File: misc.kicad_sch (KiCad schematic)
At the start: 23 parts, among them J7 Conn_ARM_JTAG_SWD_10, SW2 SW_DIP_x02, U1 MIMX8MM6DVTLZAA, Y3 24Mhz

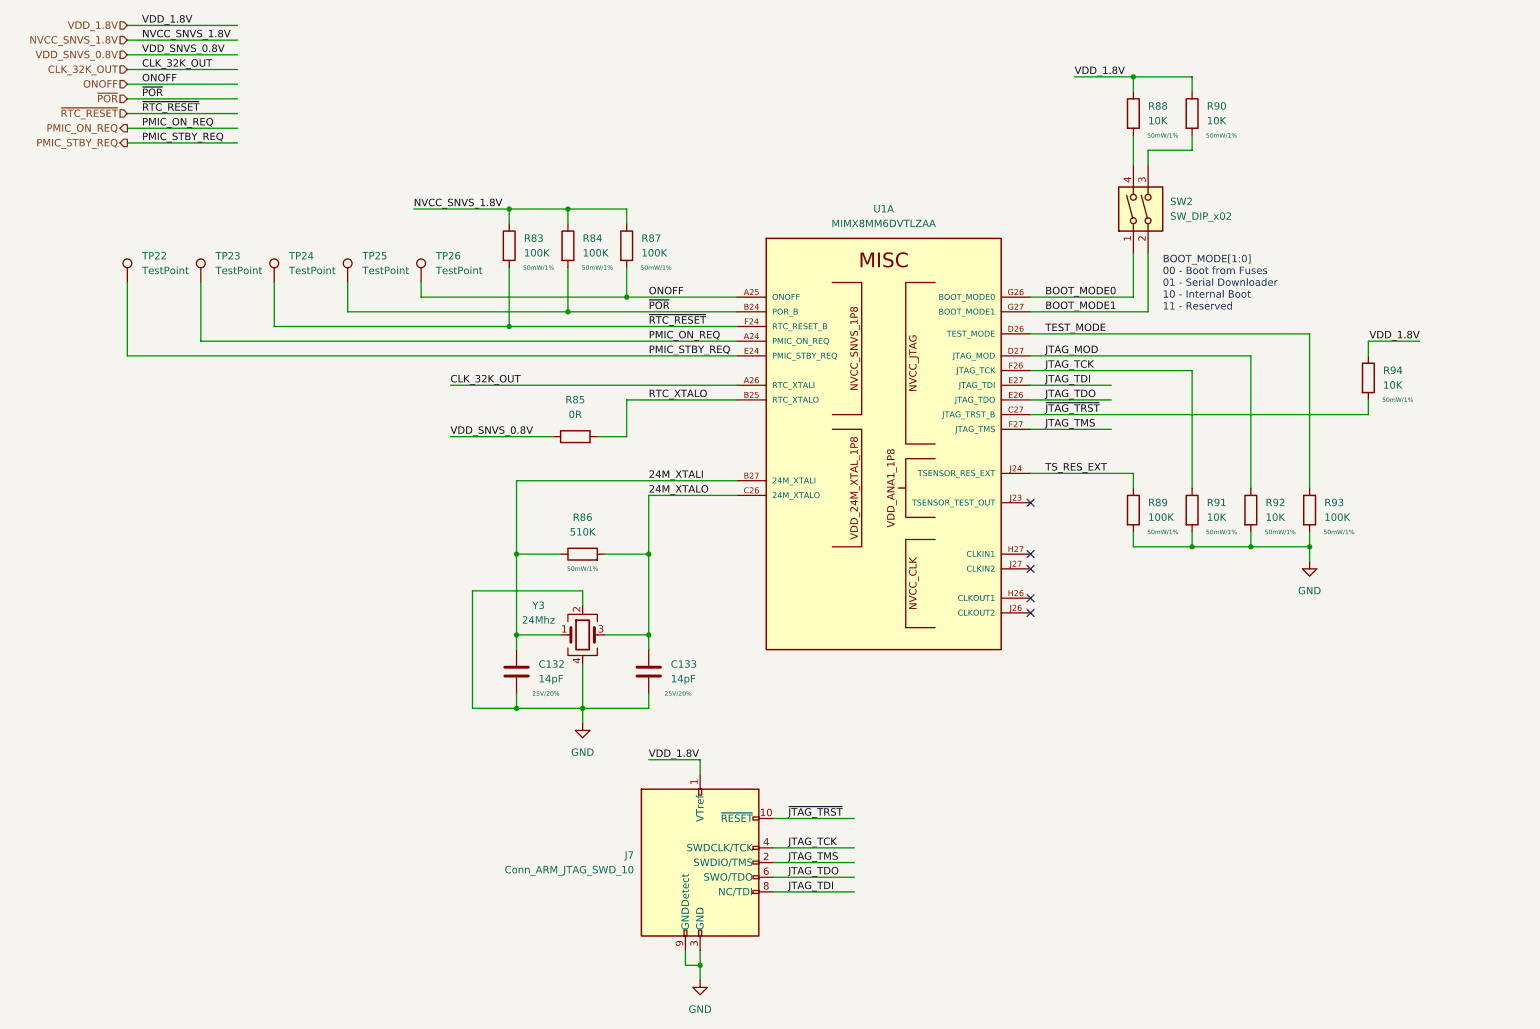
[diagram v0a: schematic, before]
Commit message: add SN65DSI86 DSI2DP ic, SCH, PCB work, flytime work
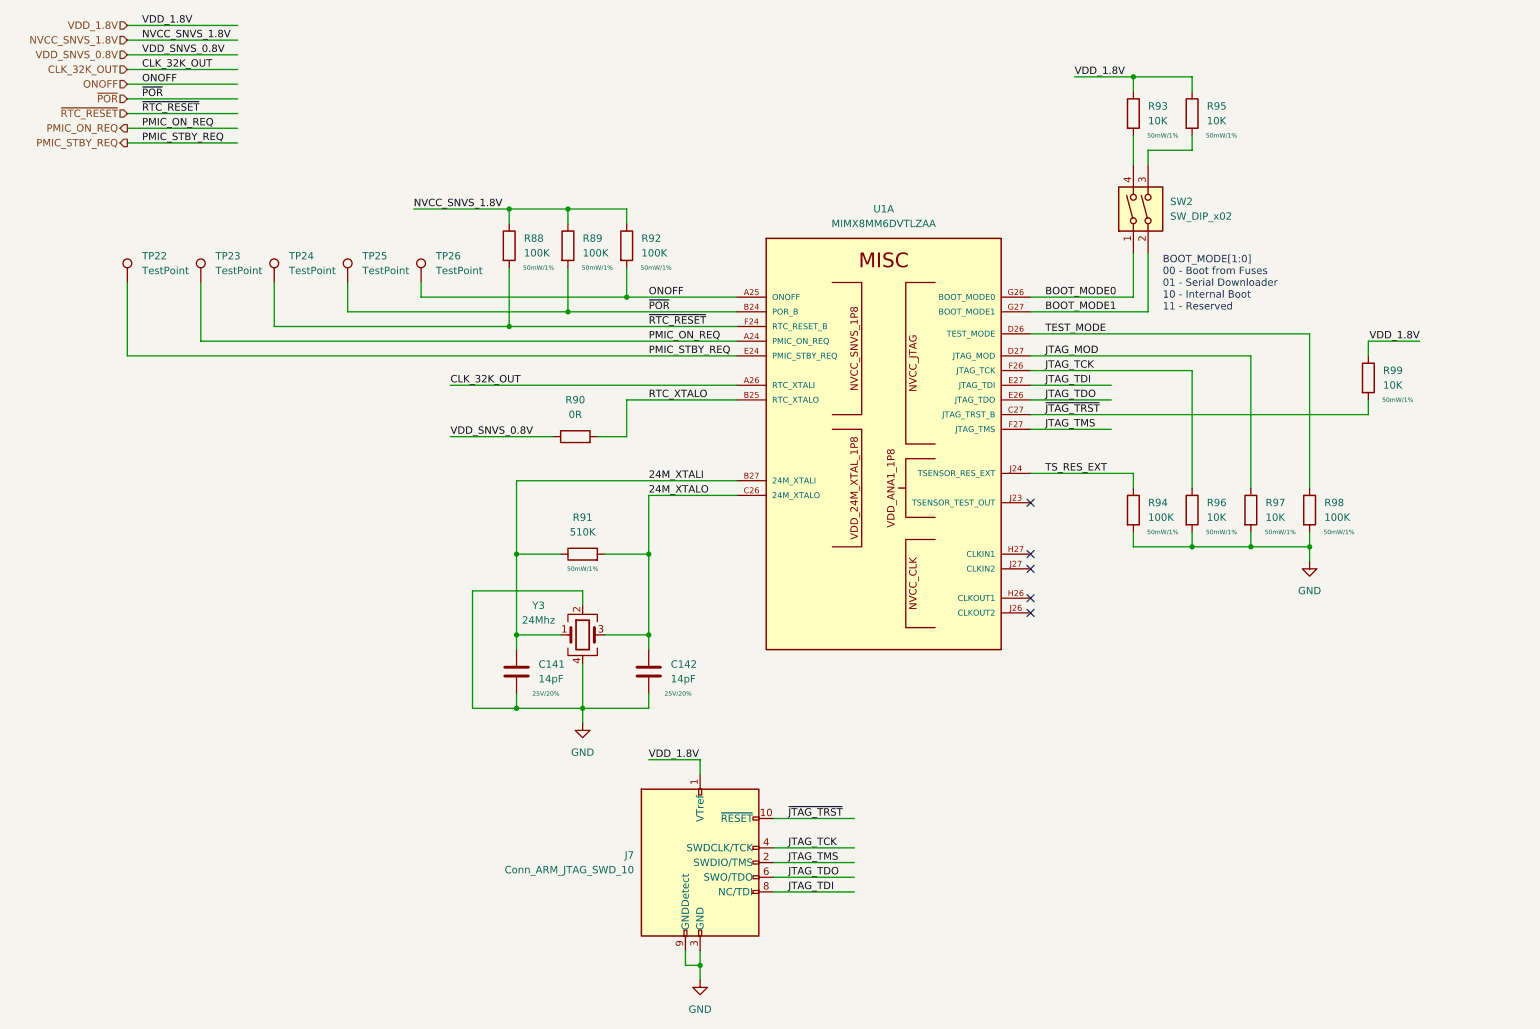
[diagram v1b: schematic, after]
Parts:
- renumbered C132 to C141, C133 to C142, R83 to R88, R84 to R89, R85 to R90, R86 to R91, R87 to R92, R88 to R93, R89 to R94, R90 to R95, R91 to R96, R92 to R97, R93 to R98, R94 to R99
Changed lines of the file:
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@@
   (symbol (lib_id "Device:C") (at 97.79 132.08 0) (unit 1)
     (in_bom yes) (on_board yes)
-    (property "Reference" "C132" (id 0) (at 101.6 130.8099 0)
+    (property "Reference" "C141" (id 0) (at 101.6 130.8099 0)
       (effects (font (size 1.27 1.27)) (justify left))
     )
@@
   (symbol (lib_id "Device:R") (at 224.79 104.14 0) (unit 1)
     (in_bom yes) (on_board yes)
-    (property "Reference" "R92" (id 0) (at 227.33 102.8699 0)
+    (property "Reference" "R97" (id 0) (at 227.33 102.8699 0)
       (effects (font (size 1.27 1.27)) (justify left))
     )
@@
   (symbol (lib_id "power:GND") (at 129.54 185.42 0) (unit 1)
     (in_bom yes) (on_board yes) (fields_autoplaced)
-    (property "Reference" "#PWR0128" (id 0) (at 129.54 191.77 0)
+    (property "Reference" "#PWR0132" (id 0) (at 129.54 191.77 0)
       (effects (font (size 1.27 1.27)) hide)
     )
@@
   (symbol (lib_id "Device:R") (at 214.63 35.56 0) (unit 1)
     (in_bom yes) (on_board yes)
-    (property "Reference" "R90" (id 0) (at 217.17 34.2899 0)
+    (property "Reference" "R95" (id 0) (at 217.17 34.2899 0)
       (effects (font (size 1.27 1.27)) (justify left))
     )
@@
   (symbol (lib_id "Device:R") (at 204.47 35.56 0) (unit 1)
     (in_bom yes) (on_board yes)
-    (property "Reference" "R88" (id 0) (at 207.01 34.2899 0)
+    (property "Reference" "R93" (id 0) (at 207.01 34.2899 0)
       (effects (font (size 1.27 1.27)) (justify left))
     )
@@
   (symbol (lib_id "Device:R") (at 96.52 58.42 0) (unit 1)
     (in_bom yes) (on_board yes)
-    (property "Reference" "R83" (id 0) (at 99.06 57.1499 0)
+    (property "Reference" "R88" (id 0) (at 99.06 57.1499 0)
       (effects (font (size 1.27 1.27)) (justify left))
     )
@@
   (symbol (lib_id "Device:R") (at 109.22 111.76 90) (unit 1)
     (in_bom yes) (on_board yes)
-    (property "Reference" "R86" (id 0) (at 109.22 105.41 90))
+    (property "Reference" "R91" (id 0) (at 109.22 105.41 90))
     (property "Value" "510K" (id 1) (at 109.22 107.95 90))
     (property "Footprint" "Resistor_SMD:R_0402_1005Metric" (id 2) (at 109.22 113.538 90)
@@
   (symbol (lib_id "power:GND") (at 109.22 140.97 0) (unit 1)
     (in_bom yes) (on_board yes) (fields_autoplaced)
-    (property "Reference" "#PWR0127" (id 0) (at 109.22 147.32 0)
+    (property "Reference" "#PWR0131" (id 0) (at 109.22 147.32 0)
       (effects (font (size 1.27 1.27)) hide)
     )
@@
   (symbol (lib_id "Device:R") (at 234.95 104.14 0) (unit 1)
     (in_bom yes) (on_board yes)
-    (property "Reference" "R93" (id 0) (at 237.49 102.8699 0)
+    (property "Reference" "R98" (id 0) (at 237.49 102.8699 0)
       (effects (font (size 1.27 1.27)) (justify left))
     )
@@
   (symbol (lib_id "Device:R") (at 214.63 104.14 0) (unit 1)
     (in_bom yes) (on_board yes)
-    (property "Reference" "R91" (id 0) (at 217.17 102.8699 0)
+    (property "Reference" "R96" (id 0) (at 217.17 102.8699 0)
       (effects (font (size 1.27 1.27)) (justify left))
     )
@@
   (symbol (lib_id "Device:R") (at 116.84 58.42 0) (unit 1)
     (in_bom yes) (on_board yes)
-    (property "Reference" "R87" (id 0) (at 119.38 57.1499 0)
+    (property "Reference" "R92" (id 0) (at 119.38 57.1499 0)
       (effects (font (size 1.27 1.27)) (justify left))
     )
@@
   (symbol (lib_id "power:GND") (at 234.95 113.03 0) (unit 1)
     (in_bom yes) (on_board yes) (fields_autoplaced)
-    (property "Reference" "#PWR0129" (id 0) (at 234.95 119.38 0)
+    (property "Reference" "#PWR0133" (id 0) (at 234.95 119.38 0)
       (effects (font (size 1.27 1.27)) hide)
     )
@@
   (symbol (lib_id "Device:R") (at 204.47 104.14 0) (unit 1)
     (in_bom yes) (on_board yes)
-    (property "Reference" "R89" (id 0) (at 207.01 102.8699 0)
+    (property "Reference" "R94" (id 0) (at 207.01 102.8699 0)
       (effects (font (size 1.27 1.27)) (justify left))
     )
@@
   (symbol (lib_id "Device:C") (at 120.65 132.08 0) (unit 1)
     (in_bom yes) (on_board yes)
-    (property "Reference" "C133" (id 0) (at 124.46 130.8099 0)
+    (property "Reference" "C142" (id 0) (at 124.46 130.8099 0)
       (effects (font (size 1.27 1.27)) (justify left))
     )
@@
   (symbol (lib_id "Device:R") (at 245.11 81.28 0) (unit 1)
     (in_bom yes) (on_board yes)
-    (property "Reference" "R94" (id 0) (at 247.65 80.0099 0)
+    (property "Reference" "R99" (id 0) (at 247.65 80.0099 0)
       (effects (font (size 1.27 1.27)) (justify left))
     )
@@
   (symbol (lib_id "Device:R") (at 106.68 58.42 0) (unit 1)
     (in_bom yes) (on_board yes)
-    (property "Reference" "R84" (id 0) (at 109.22 57.1499 0)
+    (property "Reference" "R89" (id 0) (at 109.22 57.1499 0)
       (effects (font (size 1.27 1.27)) (justify left))
     )
@@
   (symbol (lib_id "Device:R") (at 107.95 91.44 90) (unit 1)
     (in_bom yes) (on_board yes) (fields_autoplaced)
-    (property "Reference" "R85" (id 0) (at 107.95 85.09 90))
+    (property "Reference" "R90" (id 0) (at 107.95 85.09 90))
     (property "Value" "0R" (id 1) (at 107.95 87.63 90))
     (property "Footprint" "Resistor_SMD:R_0402_1005Metric" (id 2) (at 107.95 93.218 90)

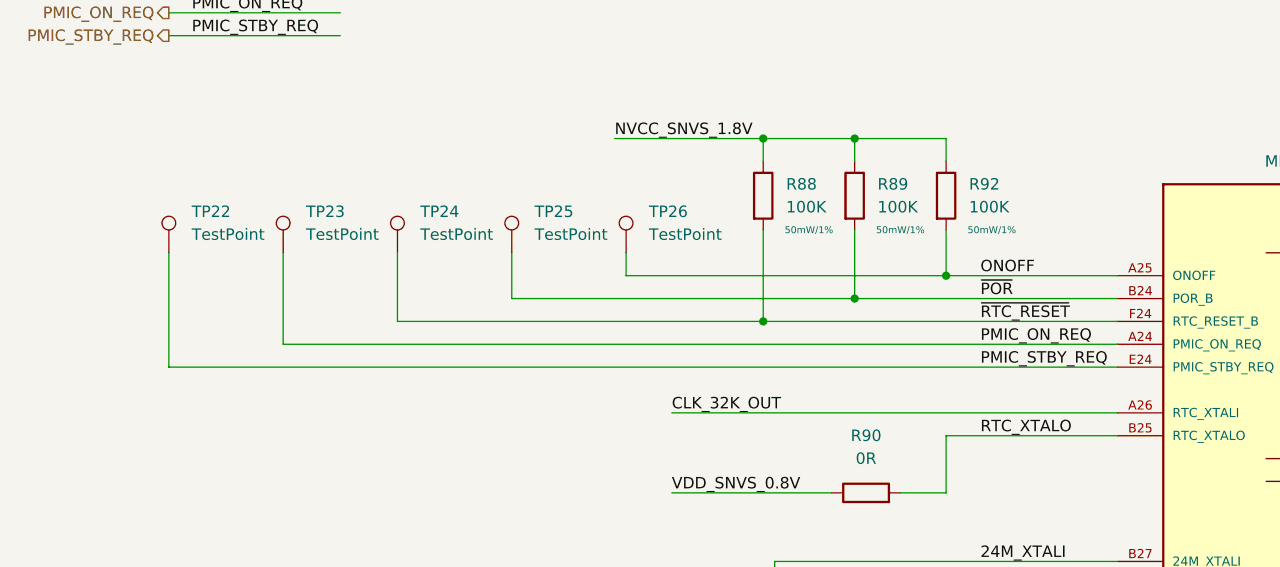
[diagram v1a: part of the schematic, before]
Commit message: add UART4 connector
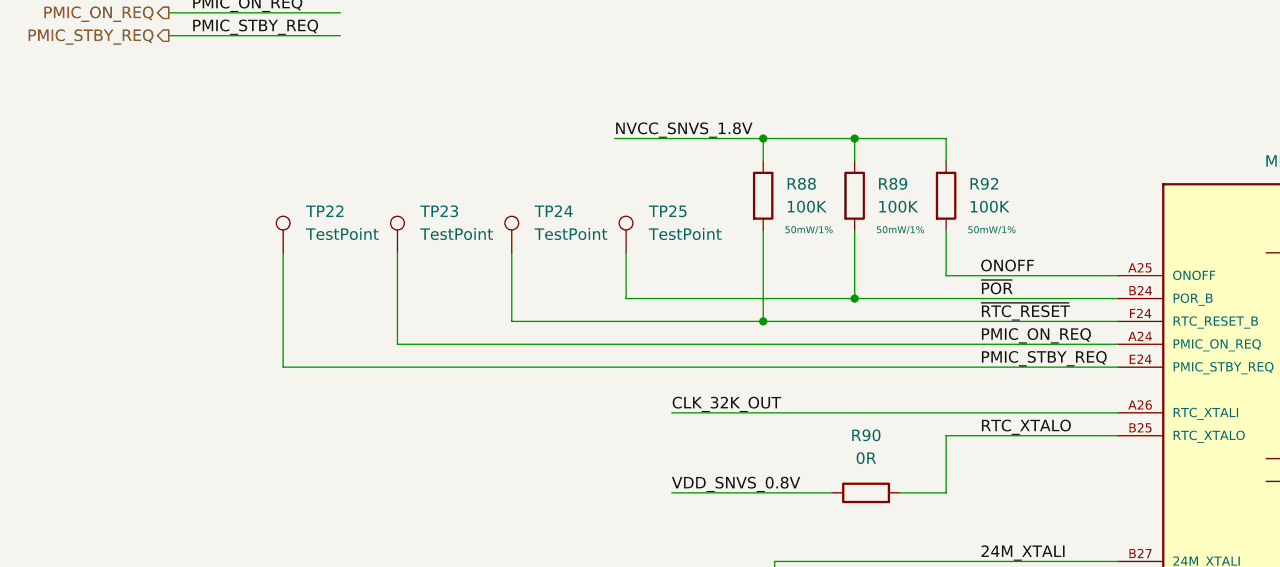
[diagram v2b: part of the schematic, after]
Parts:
- removed TP26: TestPoint, TestPoint:TestPoint_Pad_D1.0mm, symbol Connector:TestPoint
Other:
- moved on the sheet: TP22, TP23, TP24, TP25
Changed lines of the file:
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@@
   (junction (at 224.79 110.49) (diameter 0) (color 0 0 0 0)
-  )
-  (junction (at 116.84 67.31) (diameter 0) (color 0 0 0 0)
   )
   (junction (at 97.79 138.43) (diameter 0) (color 0 0 0 0)
@@
     (stroke (width 0) (type default) (color 0 0 0 0))
   )
-  (wire (pts (xy 30.48 77.47) (xy 135.89 77.47))
+  (wire (pts (xy 43.18 77.47) (xy 135.89 77.47))
     (stroke (width 0) (type default) (color 0 0 0 0))
   )
@@
     (stroke (width 0) (type default) (color 0 0 0 0))
   )
-  (wire (pts (xy 81.28 64.77) (xy 81.28 67.31))
-    (stroke (width 0) (type default) (color 0 0 0 0))
-  )
   (wire (pts (xy 97.79 111.76) (xy 105.41 111.76))
     (stroke (width 0) (type default) (color 0 0 0 0))
@@
     (stroke (width 0) (type default) (color 0 0 0 0))
   )
-  (wire (pts (xy 68.58 69.85) (xy 68.58 64.77))
+  (wire (pts (xy 81.28 69.85) (xy 81.28 64.77))
     (stroke (width 0) (type default) (color 0 0 0 0))
   )
@@
     (stroke (width 0) (type default) (color 0 0 0 0))
   )
-  (wire (pts (xy 81.28 67.31) (xy 116.84 67.31))
-    (stroke (width 0) (type default) (color 0 0 0 0))
-  )
   (wire (pts (xy 186.69 87.63) (xy 245.11 87.63))
     (stroke (width 0) (type default) (color 0 0 0 0))
@@
     (stroke (width 0) (type default) (color 0 0 0 0))
   )
-  (wire (pts (xy 43.18 74.93) (xy 135.89 74.93))
+  (wire (pts (xy 55.88 74.93) (xy 135.89 74.93))
     (stroke (width 0) (type default) (color 0 0 0 0))
   )
@@
     (stroke (width 0) (type default) (color 0 0 0 0))
   )
-  (wire (pts (xy 55.88 64.77) (xy 55.88 72.39))
+  (wire (pts (xy 68.58 64.77) (xy 68.58 72.39))
     (stroke (width 0) (type default) (color 0 0 0 0))
   )
@@
     (stroke (width 0) (type default) (color 0 0 0 0))
   )
-  (wire (pts (xy 30.48 64.77) (xy 30.48 77.47))
+  (wire (pts (xy 43.18 64.77) (xy 43.18 77.47))
     (stroke (width 0) (type default) (color 0 0 0 0))
   )
@@
     (stroke (width 0) (type default) (color 0 0 0 0))
   )
-  (wire (pts (xy 43.18 74.93) (xy 43.18 64.77))
+  (wire (pts (xy 55.88 74.93) (xy 55.88 64.77))
     (stroke (width 0) (type default) (color 0 0 0 0))
   )
@@
     (stroke (width 0) (type default) (color 0 0 0 0))
   )
-  (wire (pts (xy 106.68 69.85) (xy 68.58 69.85))
+  (wire (pts (xy 106.68 69.85) (xy 81.28 69.85))
     (stroke (width 0) (type default) (color 0 0 0 0))
   )
@@
     (stroke (width 0) (type default) (color 0 0 0 0))
   )
-  (wire (pts (xy 55.88 72.39) (xy 96.52 72.39))
+  (wire (pts (xy 68.58 72.39) (xy 96.52 72.39))
     (stroke (width 0) (type default) (color 0 0 0 0))
   )
@@
     (pin "D19")
   )
-  (symbol (lib_id "Connector:TestPoint") (at 81.28 64.77 0) (unit 1)
-    (in_bom yes) (on_board yes) (fields_autoplaced)
-    (property "Reference" "TP26" (id 0) (at 83.82 60.1979 0)
-      (effects (font (size 1.27 1.27)) (justify left))
-    )
-    (property "Value" "TestPoint" (id 1) (at 83.82 62.7379 0)
-      (effects (font (size 1.27 1.27)) (justify left))
-    )
-    (property "Footprint" "TestPoint:TestPoint_Pad_D1.0mm" (id 2) (at 86.36 64.77 0)
-      (effects (font (size 1.27 1.27)) hide)
-    )
-    (property "Datasheet" "~" (id 3) (at 86.36 64.77 0)
-      (effects (font (size 1.27 1.27)) hide)
-    )
-    (pin "1")
-  )
   (symbol (lib_id "power:GND") (at 129.54 185.42 0) (unit 1)
     (in_bom yes) (on_board yes) (fields_autoplaced)
@@
     (pin "2")
   )
-  (symbol (lib_id "Connector:TestPoint") (at 68.58 64.77 0) (unit 1)
+  (symbol (lib_id "Connector:TestPoint") (at 81.28 64.77 0) (unit 1)
     (in_bom yes) (on_board yes) (fields_autoplaced)
-    (property "Reference" "TP25" (id 0) (at 71.12 60.1979 0)
-      (effects (font (size 1.27 1.27)) (justify left))
-    )
-    (property "Value" "TestPoint" (id 1) (at 71.12 62.7379 0)
-      (effects (font (size 1.27 1.27)) (justify left))
-    )
-    (property "Footprint" "TestPoint:TestPoint_Pad_D1.0mm" (id 2) (at 73.66 64.77 0)
-      (effects (font (size 1.27 1.27)) hide)
-    )
-    (property "Datasheet" "~" (id 3) (at 73.66 64.77 0)
+    (property "Reference" "TP25" (id 0) (at 83.82 60.1979 0)
+      (effects (font (size 1.27 1.27)) (justify left))
+    )
+    (property "Value" "TestPoint" (id 1) (at 83.82 62.7379 0)
+      (effects (font (size 1.27 1.27)) (justify left))
+    )
+    (property "Footprint" "TestPoint:TestPoint_Pad_D1.0mm" (id 2) (at 86.36 64.77 0)
+      (effects (font (size 1.27 1.27)) hide)
+    )
+    (property "Datasheet" "~" (id 3) (at 86.36 64.77 0)
       (effects (font (size 1.27 1.27)) hide)
     )
@@
     (pin "1")
   )
-  (symbol (lib_id "Connector:TestPoint") (at 55.88 64.77 0) (unit 1)
+  (symbol (lib_id "Connector:TestPoint") (at 68.58 64.77 0) (unit 1)
     (in_bom yes) (on_board yes) (fields_autoplaced)
-    (property "Reference" "TP24" (id 0) (at 58.42 60.1979 0)
-      (effects (font (size 1.27 1.27)) (justify left))
-    )
-    (property "Value" "TestPoint" (id 1) (at 58.42 62.7379 0)
-      (effects (font (size 1.27 1.27)) (justify left))
-    )
-    (property "Footprint" "TestPoint:TestPoint_Pad_D1.0mm" (id 2) (at 60.96 64.77 0)
-      (effects (font (size 1.27 1.27)) hide)
-    )
-    (property "Datasheet" "~" (id 3) (at 60.96 64.77 0)
+    (property "Reference" "TP24" (id 0) (at 71.12 60.1979 0)
+      (effects (font (size 1.27 1.27)) (justify left))
+    )
+    (property "Value" "TestPoint" (id 1) (at 71.12 62.7379 0)
+      (effects (font (size 1.27 1.27)) (justify left))
+    )
+    (property "Footprint" "TestPoint:TestPoint_Pad_D1.0mm" (id 2) (at 73.66 64.77 0)
+      (effects (font (size 1.27 1.27)) hide)
+    )
+    (property "Datasheet" "~" (id 3) (at 73.66 64.77 0)
       (effects (font (size 1.27 1.27)) hide)
     )
@@
     (pin "2")
   )
-  (symbol (lib_id "Connector:TestPoint") (at 30.48 64.77 0) (unit 1)
+  (symbol (lib_id "Connector:TestPoint") (at 43.18 64.77 0) (unit 1)
     (in_bom yes) (on_board yes) (fields_autoplaced)
-    (property "Reference" "TP22" (id 0) (at 33.02 60.1979 0)
-      (effects (font (size 1.27 1.27)) (justify left))
-    )
-    (property "Value" "TestPoint" (id 1) (at 33.02 62.7379 0)
-      (effects (font (size 1.27 1.27)) (justify left))
-    )
-    (property "Footprint" "TestPoint:TestPoint_Pad_D1.0mm" (id 2) (at 35.56 64.77 0)
-      (effects (font (size 1.27 1.27)) hide)
-    )
-    (property "Datasheet" "~" (id 3) (at 35.56 64.77 0)
+    (property "Reference" "TP22" (id 0) (at 45.72 60.1979 0)
+      (effects (font (size 1.27 1.27)) (justify left))
+    )
+    (property "Value" "TestPoint" (id 1) (at 45.72 62.7379 0)
+      (effects (font (size 1.27 1.27)) (justify left))
+    )
+    (property "Footprint" "TestPoint:TestPoint_Pad_D1.0mm" (id 2) (at 48.26 64.77 0)
+      (effects (font (size 1.27 1.27)) hide)
+    )
+    (property "Datasheet" "~" (id 3) (at 48.26 64.77 0)
       (effects (font (size 1.27 1.27)) hide)
     )
@@
     (pin "4")
   )
-  (symbol (lib_id "Connector:TestPoint") (at 43.18 64.77 0) (unit 1)
+  (symbol (lib_id "Connector:TestPoint") (at 55.88 64.77 0) (unit 1)
     (in_bom yes) (on_board yes) (fields_autoplaced)
-    (property "Reference" "TP23" (id 0) (at 45.72 60.1979 0)
-      (effects (font (size 1.27 1.27)) (justify left))
-    )
-    (property "Value" "TestPoint" (id 1) (at 45.72 62.7379 0)
-      (effects (font (size 1.27 1.27)) (justify left))
-    )
-    (property "Footprint" "TestPoint:TestPoint_Pad_D1.0mm" (id 2) (at 48.26 64.77 0)
-      (effects (font (size 1.27 1.27)) hide)
-    )
-    (property "Datasheet" "~" (id 3) (at 48.26 64.77 0)
-      (effects (font (size 1.27 1.27)) hide)
-    )
+    (property "Reference" "TP23" (id 0) (at 58.42 60.1979 0)
+      (effects (font (size 1.27 1.27)) (justify left))
+    )
+    (property "Value" "TestPoint" (id 1) (at 58.42 62.7379 0)
+      (effects (font (size 1.27 1.27)) (justify left))
+    )
+    (property "Footprint" "TestPoint:TestPoint_Pad_D1.0mm" (id 2) (at 60.96 64.77 0)
+      (effects (font (size 1.27 1.27)) hide)
+    )
+    (property "Datasheet" "~" (id 3) (at 60.96 64.77 0)
+      (effects (font (size 1.27 1.27)) hide)
+    )
